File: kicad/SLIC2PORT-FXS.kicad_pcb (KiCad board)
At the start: 4 copper layers, 120 x 90 mm, 160 parts, among them J1 USB-C_PWR, J2 DC5V_IN, J5 EXPANSION, J6 UART_DBG, K1 G5V-2_DC5, K2 G5V-2_DC5, Q1 AO3401A, Q2 2N7002, Q3 2N7002, Q4 2N7002, Q5 2N7002, Q6 2N7002, SW1 RST, SW2 BOOT, U1 M5StampS3/S3A, U106 1N5819, U2 74HCT244, U45 1N4007, U49 1N4007, U55 P3100SC, U56 1N4007, U57 1N4007, U58 1N4007, U59 1N4007, U60 BZT03C82, U64 BK2125HS601-T, U79 1N5819, U82 P3100SC, U83 1N4007, U84 1N4007, U85 1N4007, U86 1N4007, U87 BZT03C82, U91 BK2125HS601-T

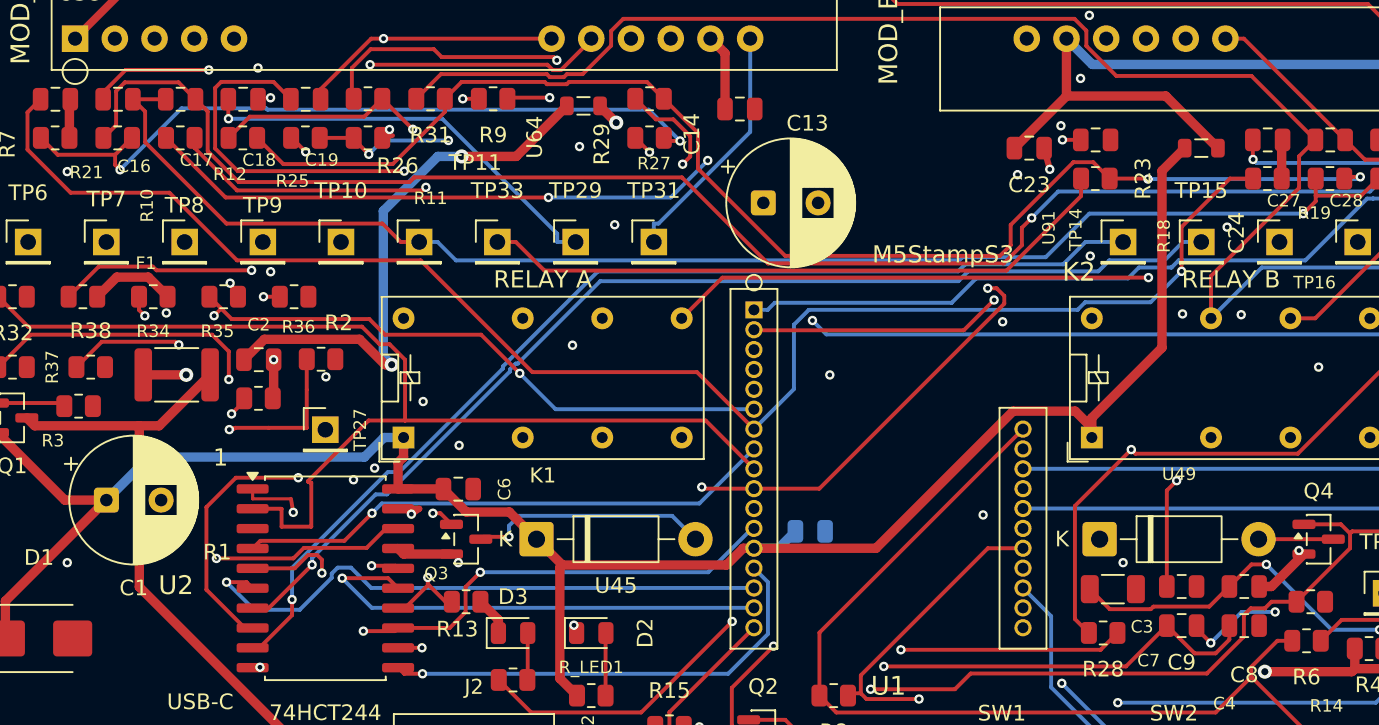
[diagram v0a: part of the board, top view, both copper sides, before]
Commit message: board v4.0 fix: GND zone clearance 0.5mm — HV netclass compliance under project-context DRC
Project-context DRC (kicad-cli inside the project, netclasses loaded) exposed 158 real violations the standalone checks could not see: HV (TIP/RING) copper vs GND pours/plane at 0.3005mm vs the HV class 0.500mm, because the GND zones were filled with 0.3mm local clearance. Fix: zone local clearance 0.3 -> 0.5mm on all three GND zones + refill; the wider carve severed six GND pour necks, reconnected with 3 stitching vias and 4 bridge tracks (connectivity analysis: all 81 GND pads back in one cluster). Final project-context DRC: 0 unconnected, 0 shorts, 216 violations, all adjudicated (104 U1 socket-intrinsic, 8 J1 footprint-intrinsic GND/VIN pad pairs at 0.200mm, 5 hand-escape marginals 0.215-0.240mm vs Power 0.25, silk groups, thermals/isolated warnings documented in CAD_REPORT round 11 addendum). HV class violations: 0. Pad-net map still identical to v3.4.2 (398 pads), hardware tests 12/12 OK. Gerbers and renders regenerated from the corrected board.
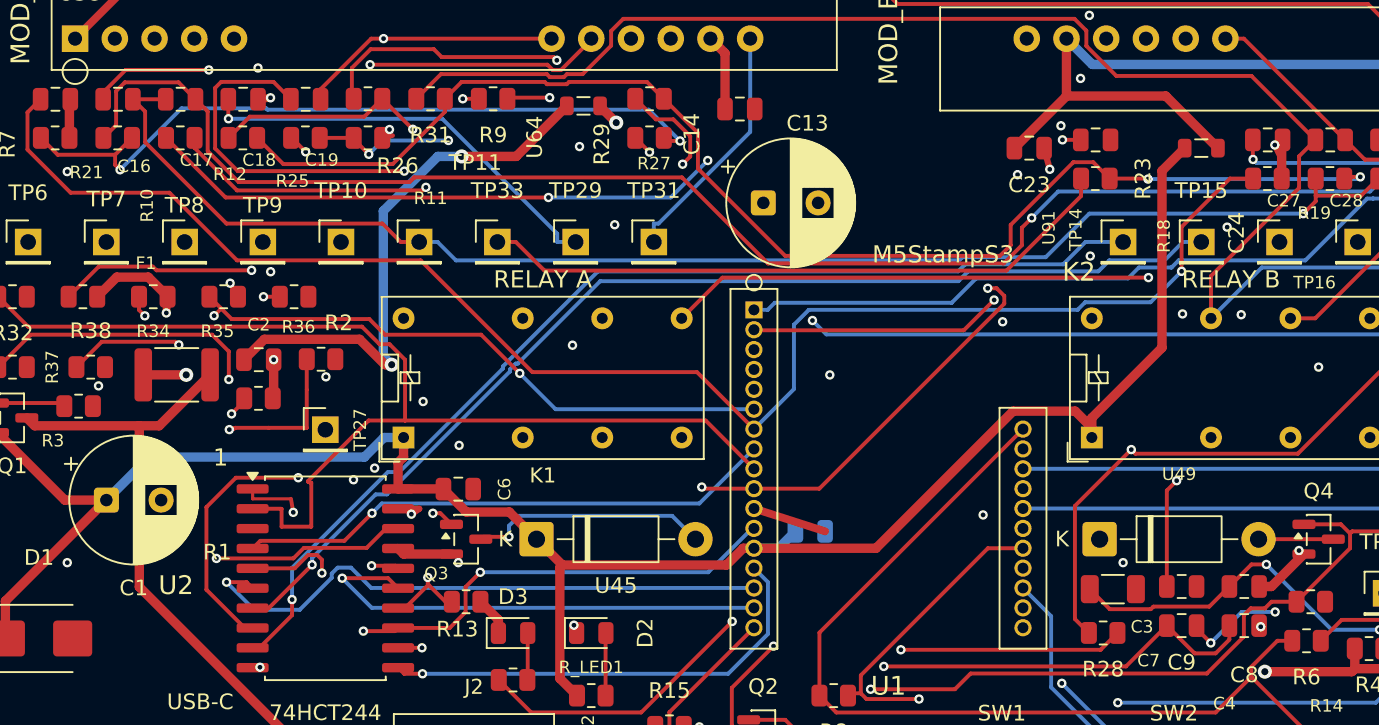
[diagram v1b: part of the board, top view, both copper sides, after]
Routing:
- net GND: track 33.8 -> 41.6 mm, vias 61 -> 64
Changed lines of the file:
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@@
 	)
 	(segment
+		(start 19.7 40.38)
+		(end 20.5 40.28)
+		(width 0.5)
+		(layer "F.Cu")
+		(net 4)
+	)
+	(segment
 		(start 12.05 88.55)
 		(end 12.6 88.8)
@@
 	)
 	(segment
+		(start 83.69 74.03)
+		(end 83.8 74.1)
+		(width 0.4)
+		(layer "F.Cu")
+		(net 4)
+	)
+	(segment
 		(start 19.35 65.92)
 		(end 21.8 65.92)
@@
 	)
 	(segment
+		(start 51.4 66.54)
+		(end 55.95 68)
+		(width 0.5)
+		(layer "F.Cu")
+		(net 4)
+	)
+	(segment
 		(start 19.35 65.5)
 		(end 19.35 65.92)
@@
 	)
 	(segment
+		(start 85.14 44.2)
+		(end 84.7 43.3)
+		(width 0.4)
+		(layer "F.Cu")
+		(net 4)
+	)
+	(segment
 		(start 29.005 69.45)
 		(end 28.65 69.095)
@@
 	)
 	(segment
+		(start 13.91 53)
+		(end 13.83 54.04)
+		(width 0.5)
+		(layer "F.Cu")
+		(net 4)
+	)
+	(segment
 		(start 20.695 59.4375)
 		(end 20.695 57.025)
@@
 	)
 	(via
+		(at 84.7 43.3)
+		(size 0.6)
+		(drill 0.3)
+		(layers "F.Cu" "B.Cu")
+		(net 4)
+	)
+	(via
 		(at 102.1 49.7)
 		(size 0.6)
@@
 	)
 	(via
+		(at 83.8 74.1)
+		(size 0.6)
+		(drill 0.3)
+		(layers "F.Cu" "B.Cu")
+		(net 4)
+	)
+	(via
 		(at 56.25 58)
 		(size 0.6)
@@
 	)
 	(via
+		(at 9.5 58.7)
+		(size 0.6)
+		(drill 0.3)
+		(layers "F.Cu" "B.Cu")
+		(net 4)
+	)
+	(via
 		(at 72.2805 39.043252)
 		(size 0.6)
@@
 		(hatch edge 0.5)
 		(connect_pads
-			(clearance 0.3)
+			(clearance 0.5)
 		)
 		(min_thickness 0.15)
@@
 		(hatch edge 0.5)
 		(connect_pads
-			(clearance 0.3)
+			(clearance 0.5)
 		)
 		(min_thickness 0.15)
@@
 		(hatch edge 0.5)
 		(connect_pads
-			(clearance 0.3)
+			(clearance 0.5)
 		)
 		(min_thickness 0.25)

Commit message: board v4.0: シルクロゴを案B (HANDSET RING) に差し替え
仮置き枠+LOGOテキストを削除し、design/logo/logo-b.svg と同一形状の
シルク図形 (gr_poly x2, union済み) を配置。幅21mm・中心(104,59.9)。
上下の R20/TP30 リファレンス文字との干渉を避けるため仮置き枠より
僅かに縮小+下方配置。DRC (プロジェクト文脈) はベースライン 216件と
カテゴリ別件数まで完全一致し、新規シルク違反なし。
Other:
- board text removed: "LOGO"
